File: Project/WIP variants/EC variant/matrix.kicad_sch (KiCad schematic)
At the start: 37 parts

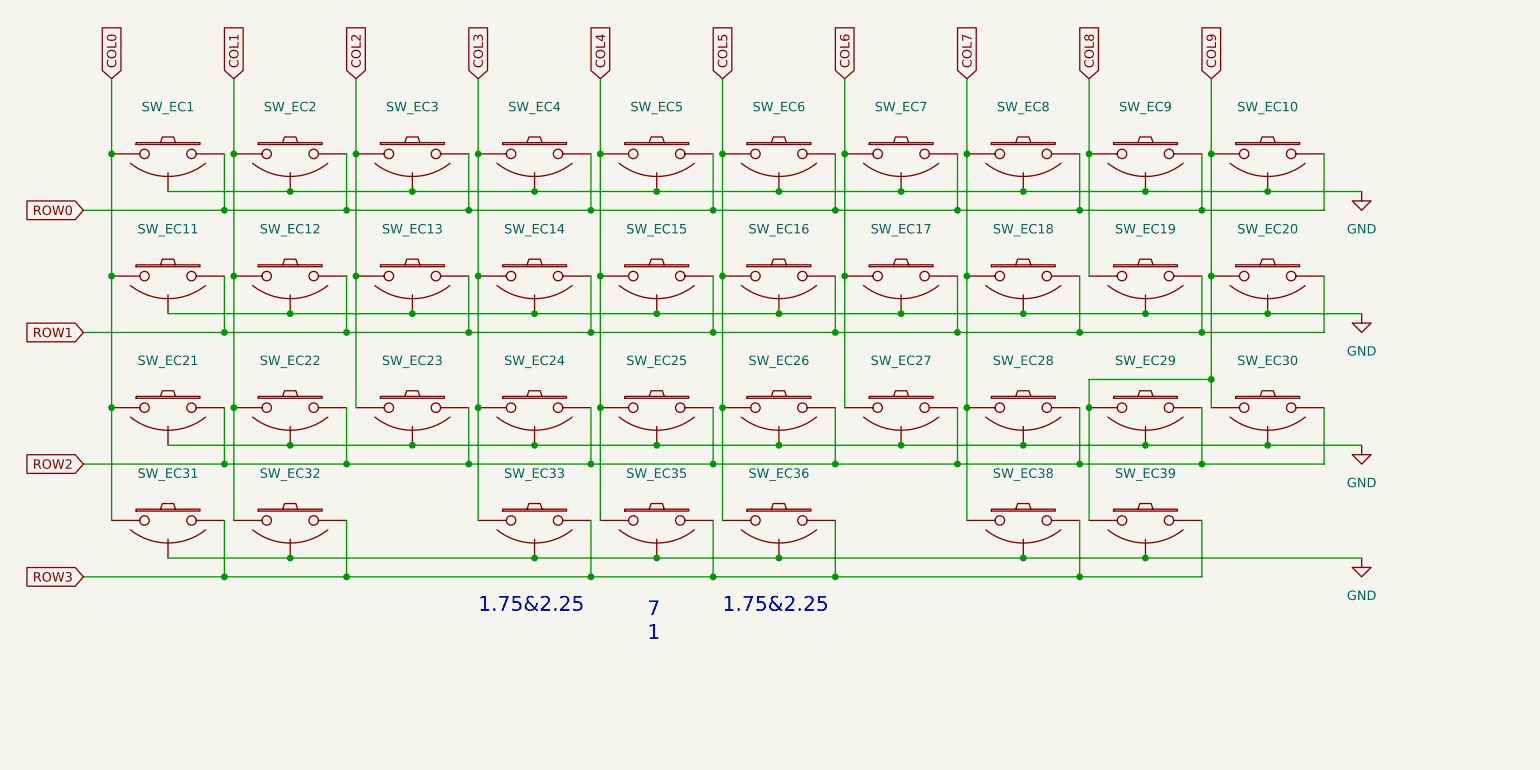
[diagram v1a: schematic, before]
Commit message: EC 2 layer production files
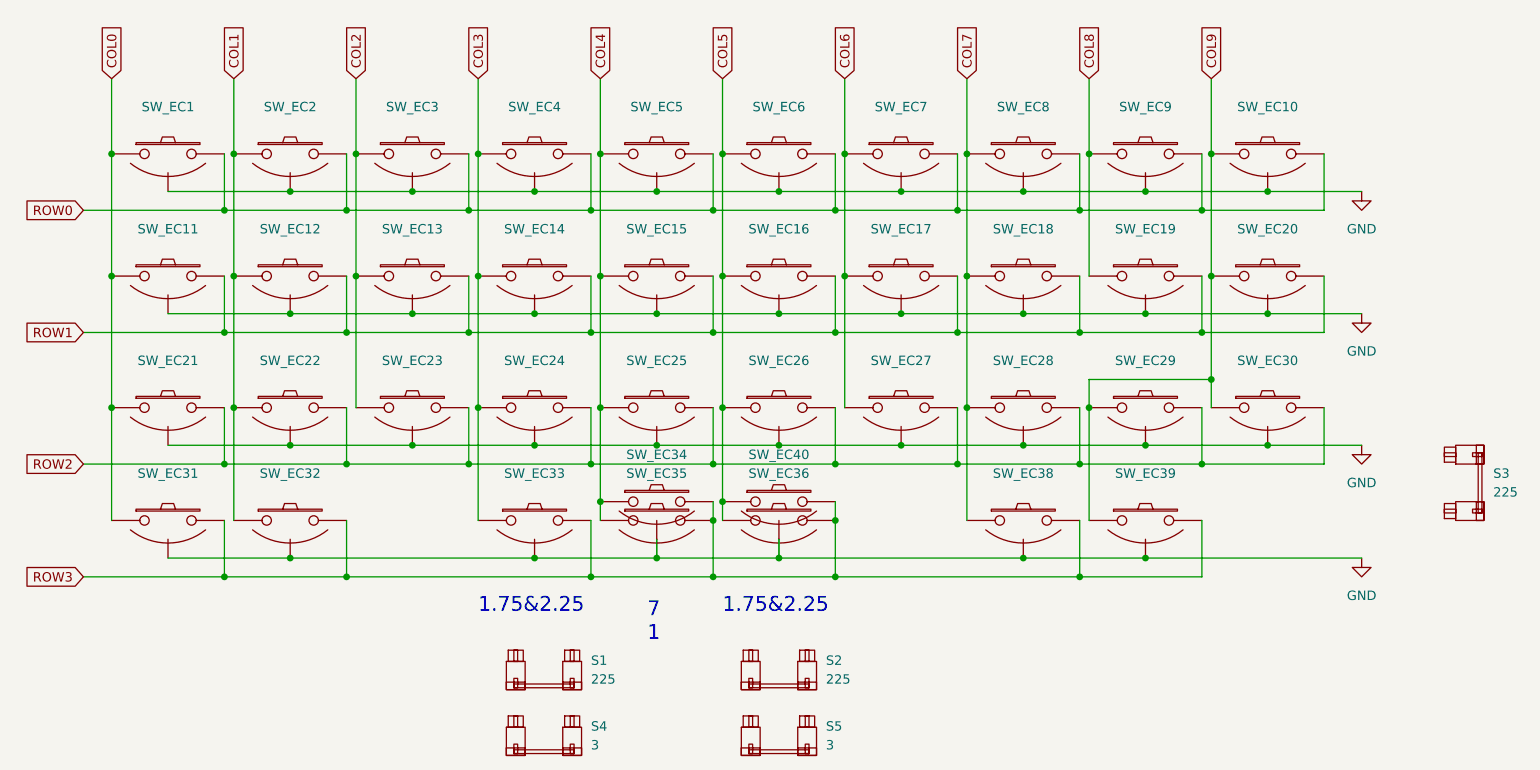
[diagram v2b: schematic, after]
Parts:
- added S1, S2: 225, PCM_marbastlib-mx:STAB_MX_2.25u, symbol PCM_marbastlib-mx:MX_stab
- added S3: 225, PCM_marbastlib-mx:STAB_MX_ISO-ROT, symbol PCM_marbastlib-mx:MX_stab
- added S4, S5: 3, PCM_marbastlib-mx:STAB_MX_3u, symbol PCM_marbastlib-mx:MX_stab
- added SW_EC34: Topre, cipulot_parts:ecs_pad_1U_no_ring_1u_edge_cut_horizontal, symbol cipulot_parts:EC_SW
- added SW_EC40: Topre, cipulot_parts:ecs_pad_1U_no_ring, symbol cipulot_parts:EC_SW
- SW_EC32: footprint cipulot_parts:ecs_pad_1U_no_ring -> cipulot_parts:ecs_pad_no_ring_1u&1.25u&1.5u
- SW_EC33: footprint cipulot_parts:ecs_pad_no_ring_stepped&normal -> cipulot_parts:ecs_pad_0.25U_0.125U_spaced_no_ring_cut_right
- SW_EC36: footprint cipulot_parts:ecs_pad_no_ring_stepped&normal -> cipulot_parts:ecs_pad_no_ring_stepped&normal_cut
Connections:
- net COL4: now also SW_EC34.1
- net COL5: now also SW_EC40.1
- net GND: now also SW_EC34.3 (SG), SW_EC40.3 (SG)
- net ROW3: now also SW_EC34.2, SW_EC40.2
